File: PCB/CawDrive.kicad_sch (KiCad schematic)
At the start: 63 parts, among them CN2 WAFER-SH1.0-6PWB, CN3 WAFER-SH1.0-4PWB, U1 TJA1051T/3/1J, U10 WAFER-SH1.0-2PWB, U11 WAFER-SH1.0-2PWB, U12 WAFER-SH1.0-2PWB, U5 WAFER-SH1.0-2PWB, U6 WAFER-SH1.0-2PWB, U8 STM32F446RETx, U9 MT6835GT-STD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

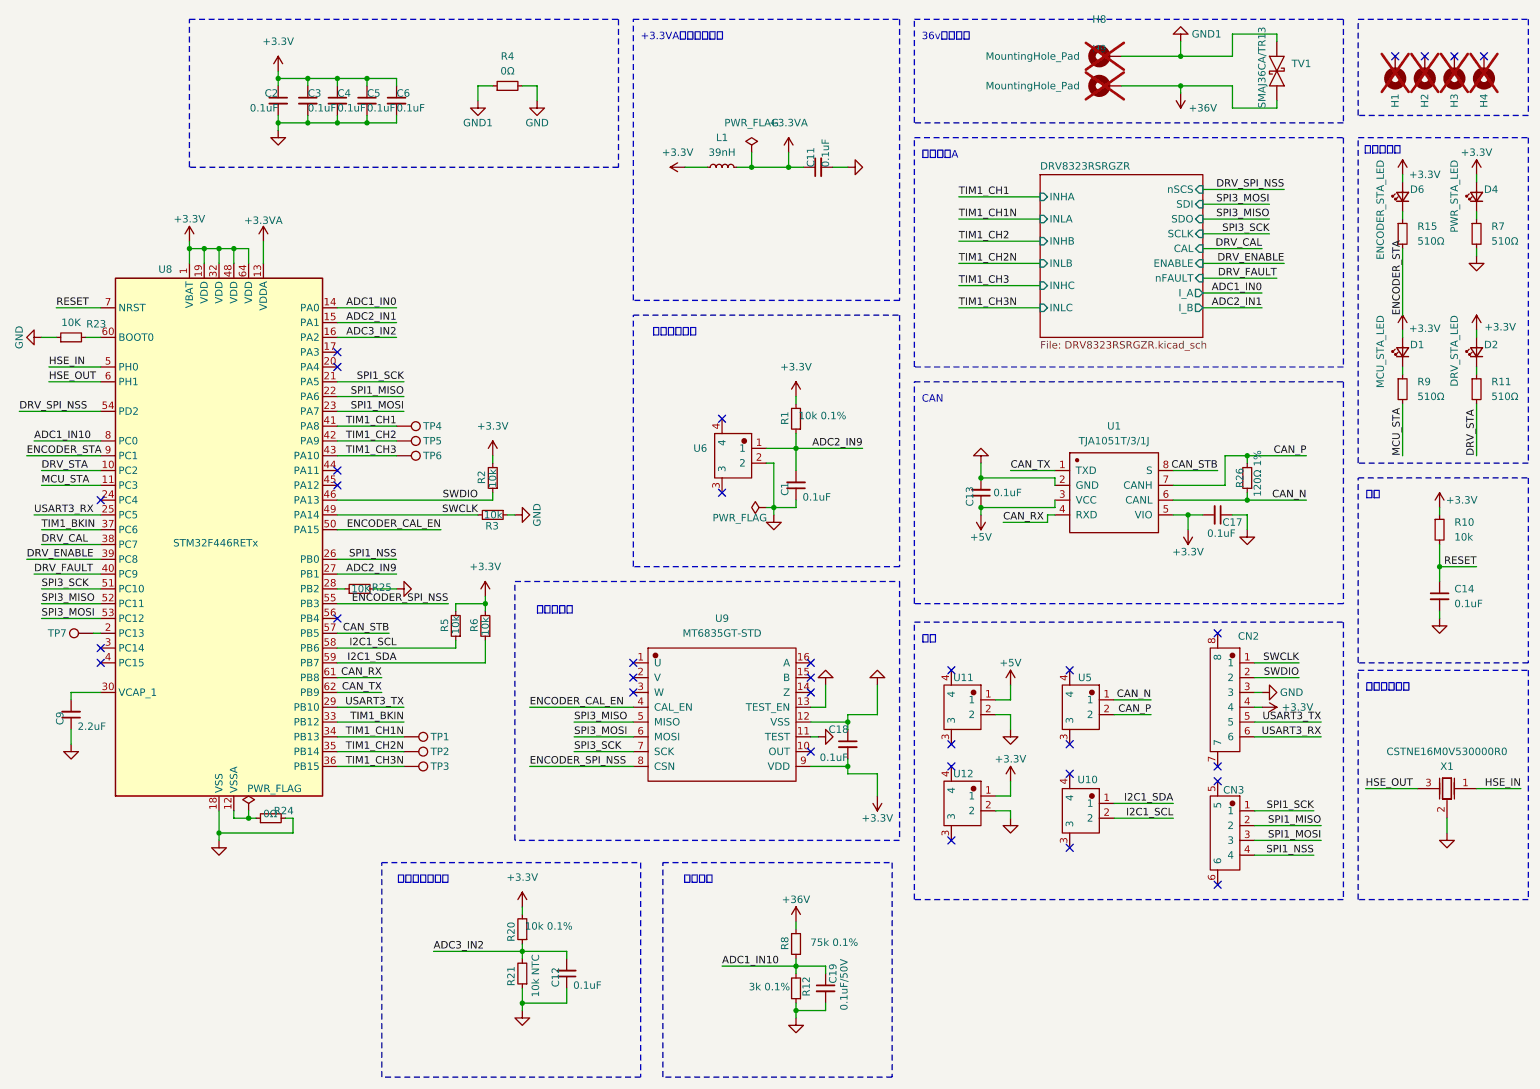
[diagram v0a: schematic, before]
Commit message: 完成FOC速度闭环控制
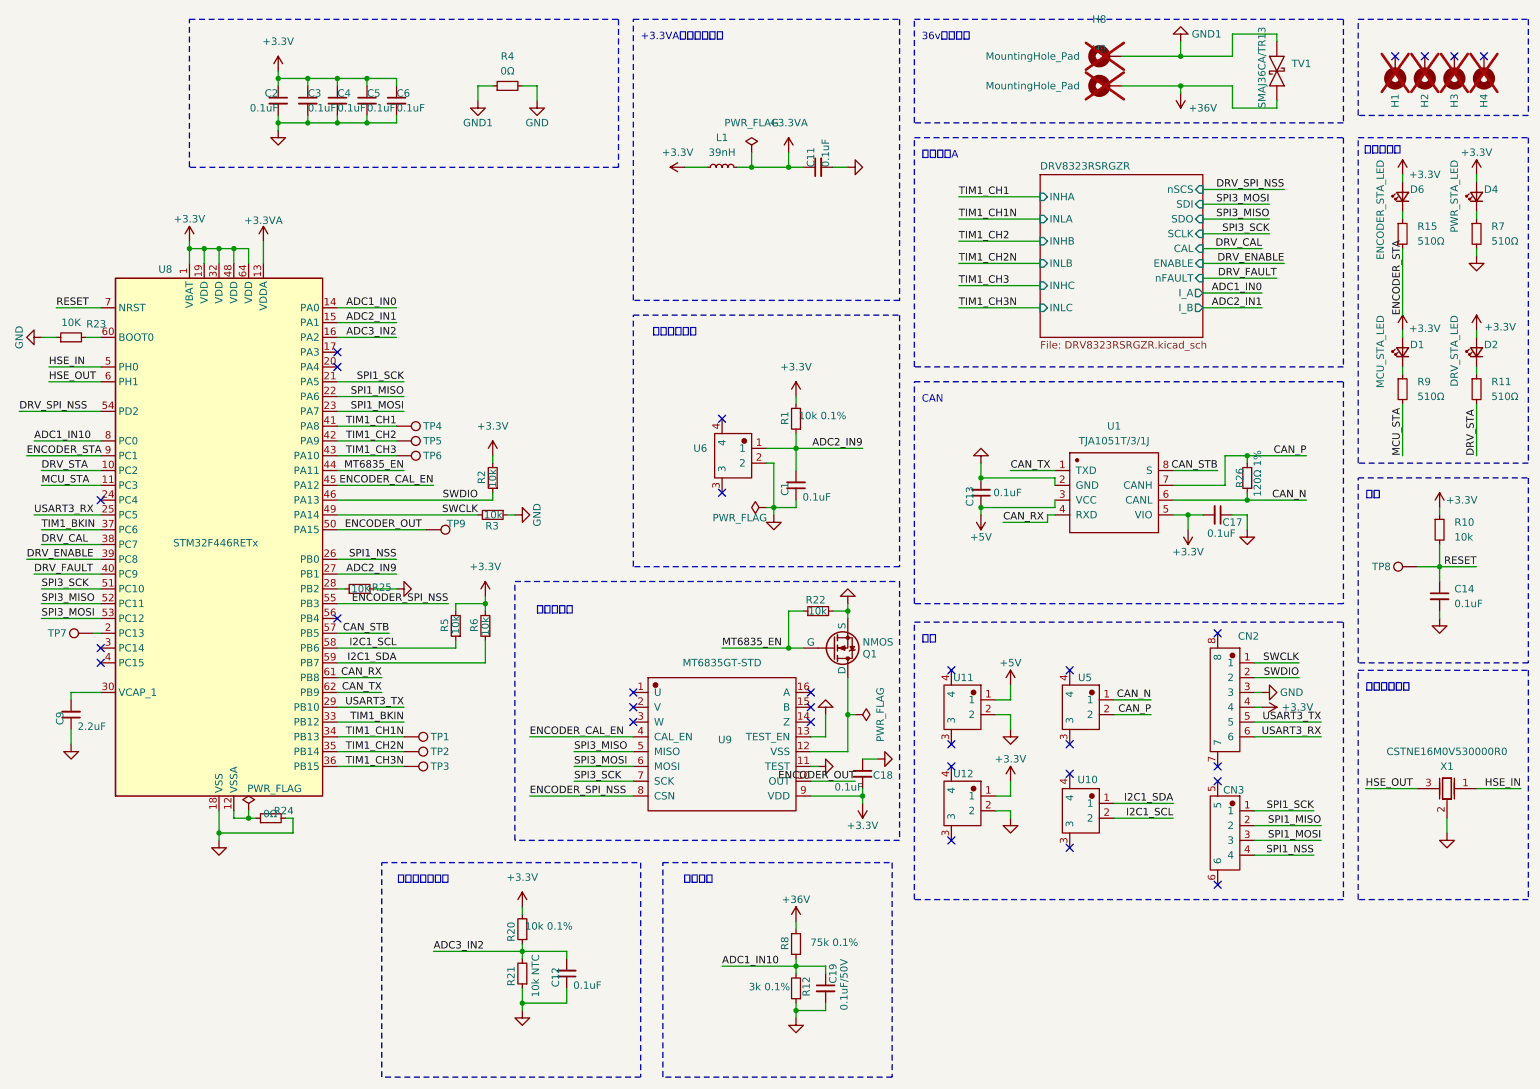
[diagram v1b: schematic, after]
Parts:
- added Q1: NMOS, Package_TO_SOT_SMD:SOT-723, symbol Simulation_SPICE:NMOS
- added R22: 10k, Resistor_SMD:R_0402_1005Metric_Pad0.72x0.64mm_HandSolder, symbol Device:R_Small
- added TP8, TP9: TestPoint, TestPoint:TestPoint_Pad_D1.0mm, symbol Connector:TestPoint
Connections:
- net ENCODER_CAL_EN: now also U8.45 (PA12); no longer U8.50 (PA15)
- net GND: now also Q1.3 (S), R22.2; no longer U9.12 (VSS)
- net RESET: now also TP8.1
- net MT6835_EN: now reaches U8.44 (PA11)
- net MT6835_EN: now also Q1.2 (G), R22.1
- net ENCODER_OUT: now reaches U9.10 (OUT)
- net ENCODER_OUT: now also U8.50 (PA15), TP9.1
- new net: Q1.1 (D), U9.12 (VSS)
- no-connect marks 33 -> 30
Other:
- moved on the sheet: C18, U9

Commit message: 增加编码器复位功能
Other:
- note added: "MT6835_EN的NMOS型号为：WNM2030 选择低导通电阻的"
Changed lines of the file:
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@@
+		)
+	)
+	(text "MT6835_EN的NMOS型号为：WNM2030\n选择低导通电阻的"
+		(exclude_from_sim no)
+		(at 128.27 118.364 0)
+		(effects
+			(font
+				(size 1.27 1.27)
+			)
 		)
 	)
